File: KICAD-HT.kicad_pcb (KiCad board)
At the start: 2 copper layers, 80 x 60 mm, 126 parts, among them J1 HV80_IN, J2 NAPPE_FILAMENT_HT, Q1 IPD050N10N5, Q2 IPD050N10N5, Q3 BSS127I, Q4 MMBT2222, Q5 BSS127I, T1 MSD1514-103ME, U1 UCC27517, U10 ISO7710, U11 AMC0311R, U12 UCC24612, U13 SN74LVC1G08, U14 TSV791, U15 ATL431, U16 LMV7219, U17 SN74LVC1G132, U18 SN74LVC1G74, U19 ISO7710F, U3 ISO7710, U5 DPC817, U7 AMC0311R, U8 AMC0311R, U9 AMC0302R

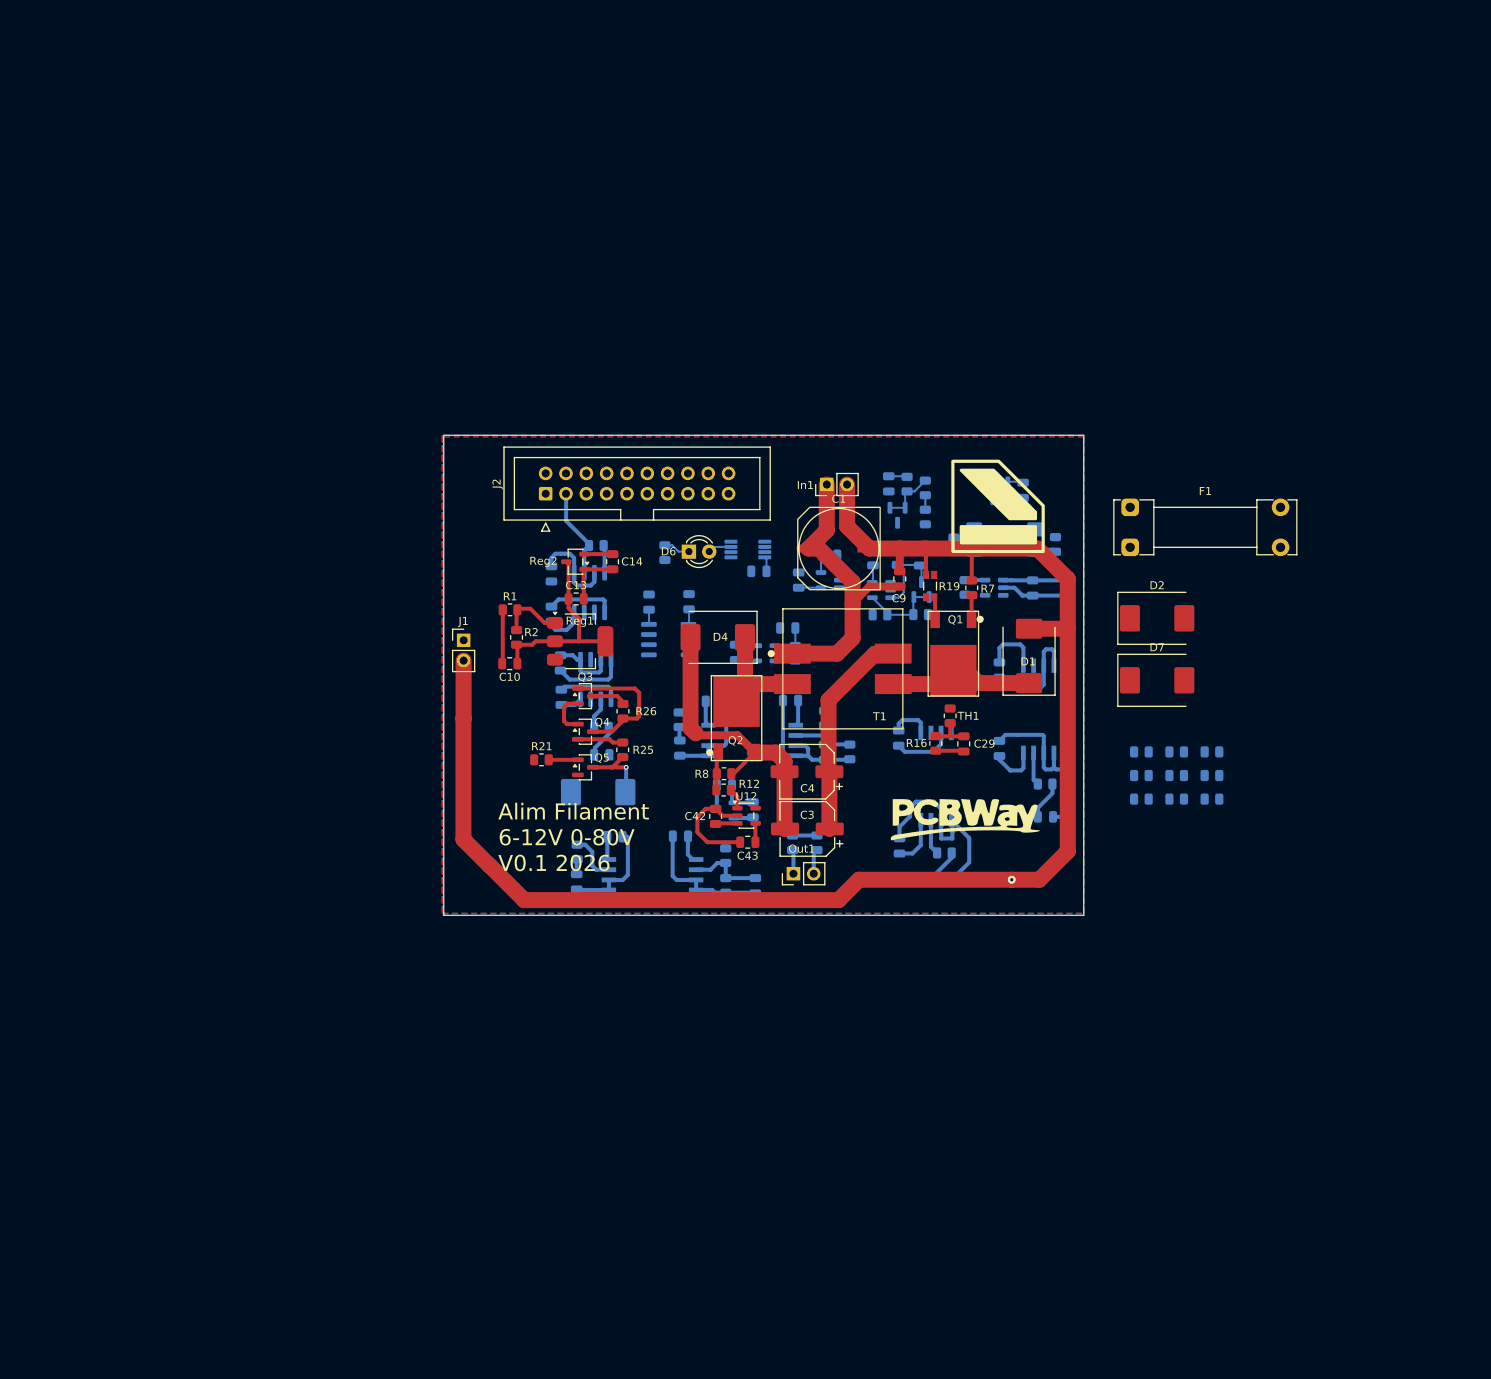
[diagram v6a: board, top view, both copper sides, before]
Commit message: Corrige la contrainte d'isolation a 4mm (ISO7710 D-8 = Basic, pas Reinforced)
Verifie dans iso7710.pdf (S5.6) : le boitier D-8 (SOIC-8 etroit) reellement
monte pour U3/U10/U19 est explicitement classe "Basic Insulation",
CLR/CPG=4mm -- le renforce 8,5mm n'existe que sur la variante DW-16, non
montee. Les AMC0302R/AMC0311R (U8/U9/U11) restent en boitier large
reinforced, DPC817 (U5) mesure a ~5mm. Barriere entiere alignee sur 4mm
(uniforme) plutot que varier par composant.

Ajoute la regle .kicad_dru "meme_composant" (A.Reference == B.Reference)
en exception avant la regle generale de barriere, necessaire car les 7
isolateurs violeraient sinon la contrainte a leurs propres broches --
syntaxe a confirmer par un DRC avant de s'y fier (non trouvee dans une
source officielle KiCad 10 aussi directe que souhaite).

Co-Authored-By: Claude Sonnet 5 <noreply@anthropic.com>
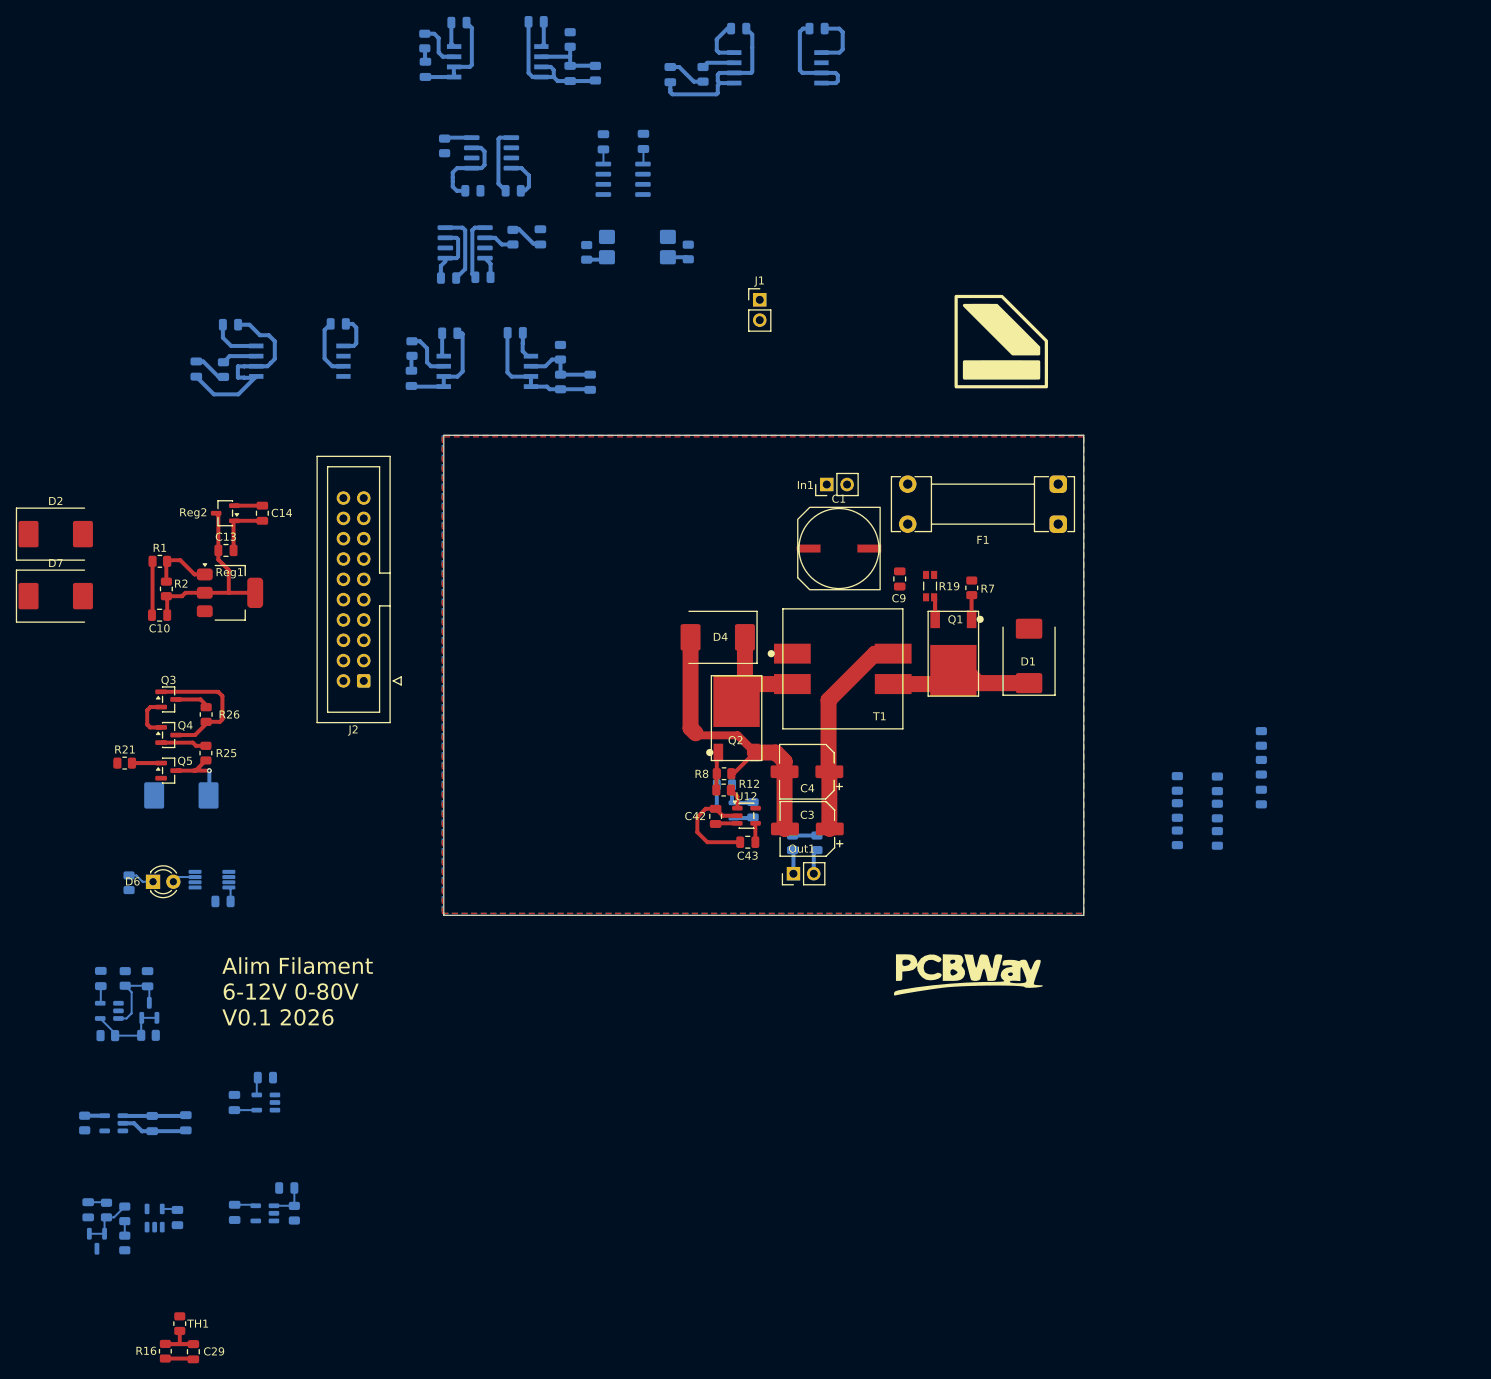
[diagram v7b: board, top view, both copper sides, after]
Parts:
- moved C46 139.4 mm to (39.7, 167.8)
- moved U13 139.4 mm to (36.9, 167.8)
- moved D2 138.1 mm to (24.5, 82.3)
- moved D7 138.1 mm to (24.5, 90.1)
- moved C55 135.1 mm to (28.6, 166.8)
- moved R30 135.1 mm to (30.8, 166.8)
- moved R31 135.1 mm to (33.1, 167.3)
- moved R32 135.1 mm to (33.1, 171.0)
- moved U15 135.1 mm to (29.6, 170.7)
- moved C19 128.8 mm to (36.6, 156.0)
- moved U1 128.8 mm to (31.8, 156.0)
- moved C21 128.8 mm to (40.8, 155.9)
- moved R11 128.8 mm to (28.1, 156.0)
- moved C29 122.7 mm to (41.7, 184.6)
- moved R16 122.7 mm to (38.2, 184.5)
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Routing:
- net GND: track 269.7 -> 81.5 mm, vias 1 -> 0
- net VIN: track 38.3 -> 0.00 mm
- net PWM_ht: track 11.3 -> 0.00 mm

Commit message: Cree les classes de nets CTRL/PRI et le fichier .kicad_dru (regle corrigee)
Ajoute les classes CTRL/PRI dans KICAD-HT.kicad_pro avec 40 nets assignes,
verifies un par un via export netlist (pas par motif de nom suppose).
Ajoute KICAD-HT.kicad_dru avec la regle de barriere a 4mm.

Corrige au passage la regle elle-meme : une regle d'exception separee
pour "meme composant" (A.Reference == B.Reference, testee aussi avec 8
regles explicites par isolateur) ne fonctionne pas -- verifie par DRC
reel, 139 violations identiques avant/apres. L'exclusion doit etre dans
la condition de la regle de barriere elle-meme (A.Reference !=
B.Reference) : 139 -> 36 violations mesure apres correction. Documente
dans doc/plan-isolation-4couches.md et regles-pcb-V2/06-haute-tension.md
(HT-10), qui contenaient la version qui ne marche pas.

Co-Authored-By: Claude Sonnet 5 <noreply@anthropic.com>
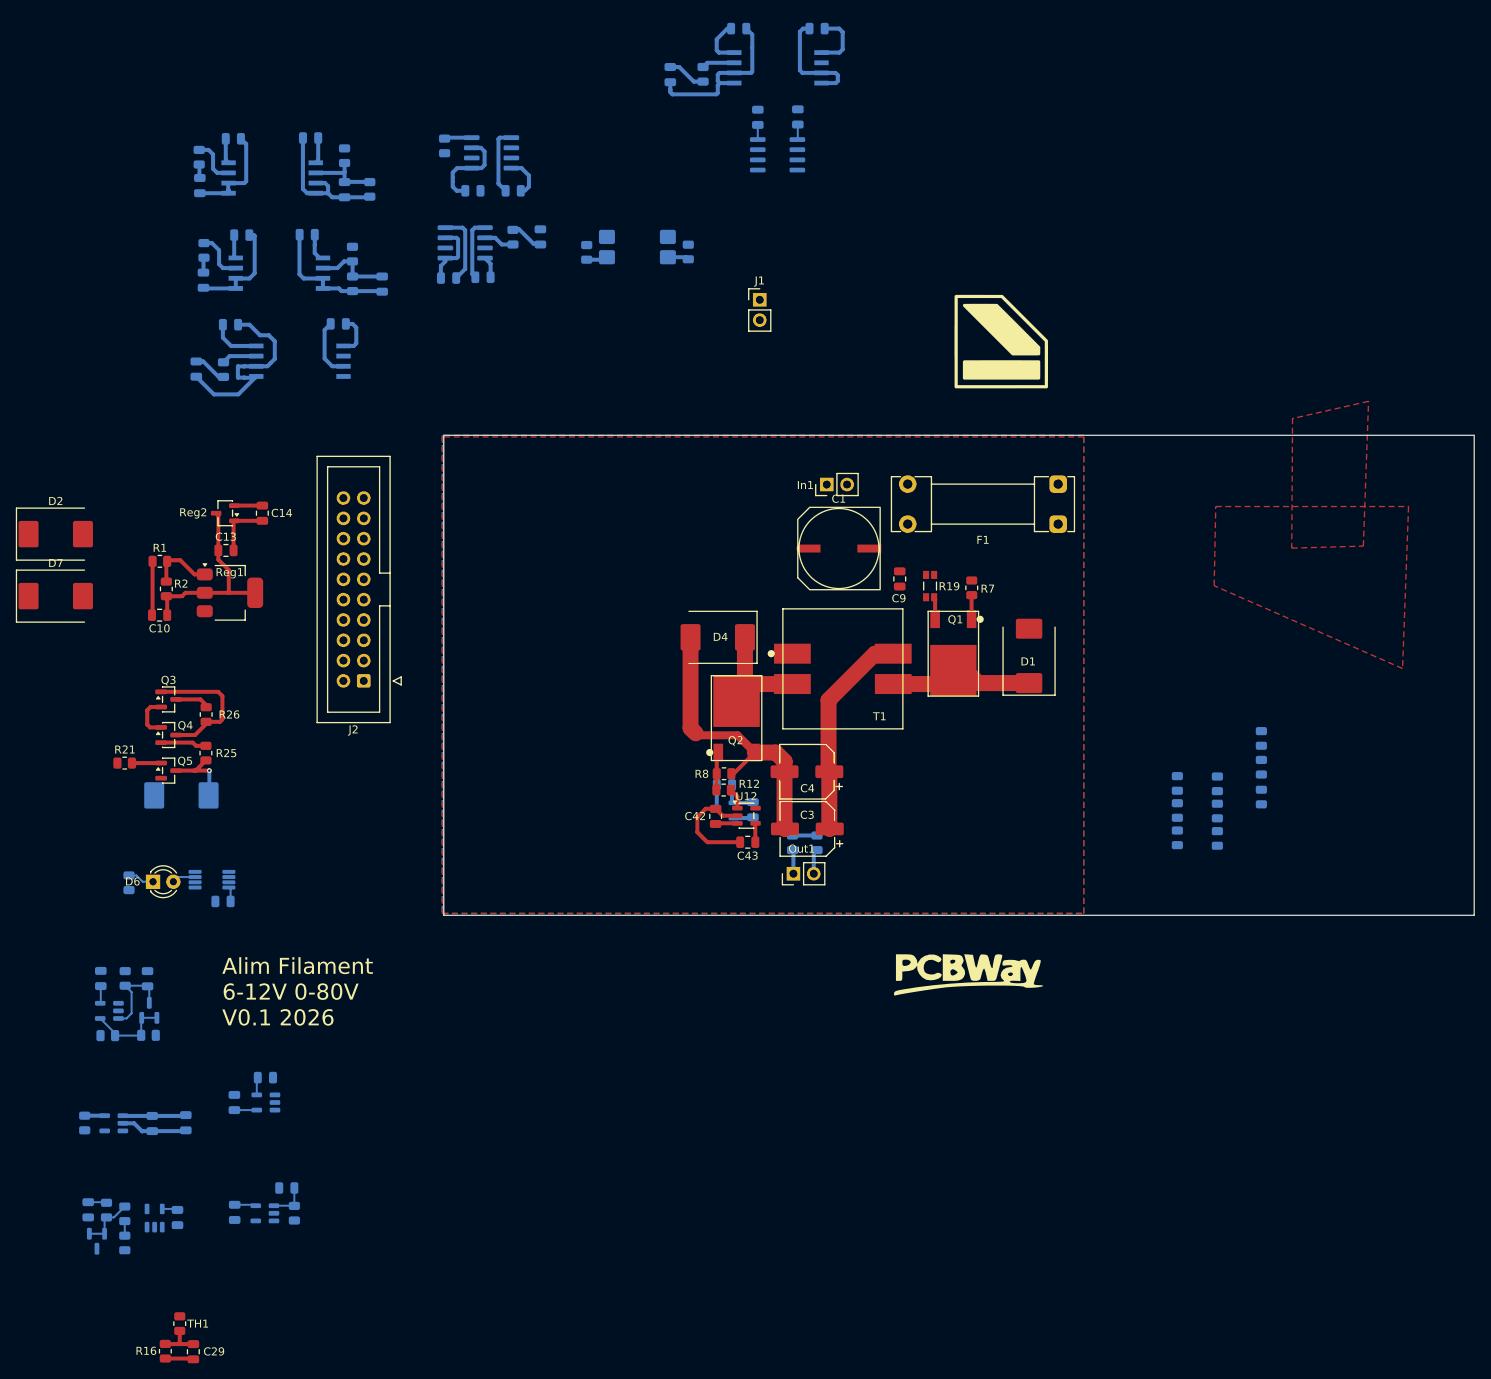
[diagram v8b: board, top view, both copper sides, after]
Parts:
- moved C39 31.7 mm to (46.7, 32.9)
- moved C41 31.7 mm to (42.5, 38.8)
- moved R24 31.7 mm to (42.4, 35.2)
- moved U11 31.7 mm to (51.5, 37.8)
- moved R23 31.7 mm to (63.8, 39.3)
- moved C38 31.7 mm to (56.4, 32.8)
- moved C40 31.7 mm to (60.6, 39.3)
- moved R22 31.7 mm to (60.6, 35.0)
- moved R13 28.7 mm to (61.6, 47.3)
- moved R15 28.7 mm to (43.0, 46.9)
- moved C23 28.7 mm to (65.3, 51.1)
- moved C24 28.7 mm to (43.0, 50.6)
- moved C28 28.7 mm to (47.8, 45.0)
- moved U7 28.7 mm to (52.5, 49.7)
- moved C18 28.7 mm to (55.9, 44.9)
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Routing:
- added copper zone on F.Cu, net GND_CTRL
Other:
- board size 80 x 60 mm -> 128.8 x 60 mm
